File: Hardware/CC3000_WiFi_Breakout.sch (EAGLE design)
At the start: 31 parts, among them J1 U.FL, U1 LM1117, U3 74HC4050, U5 CC3000

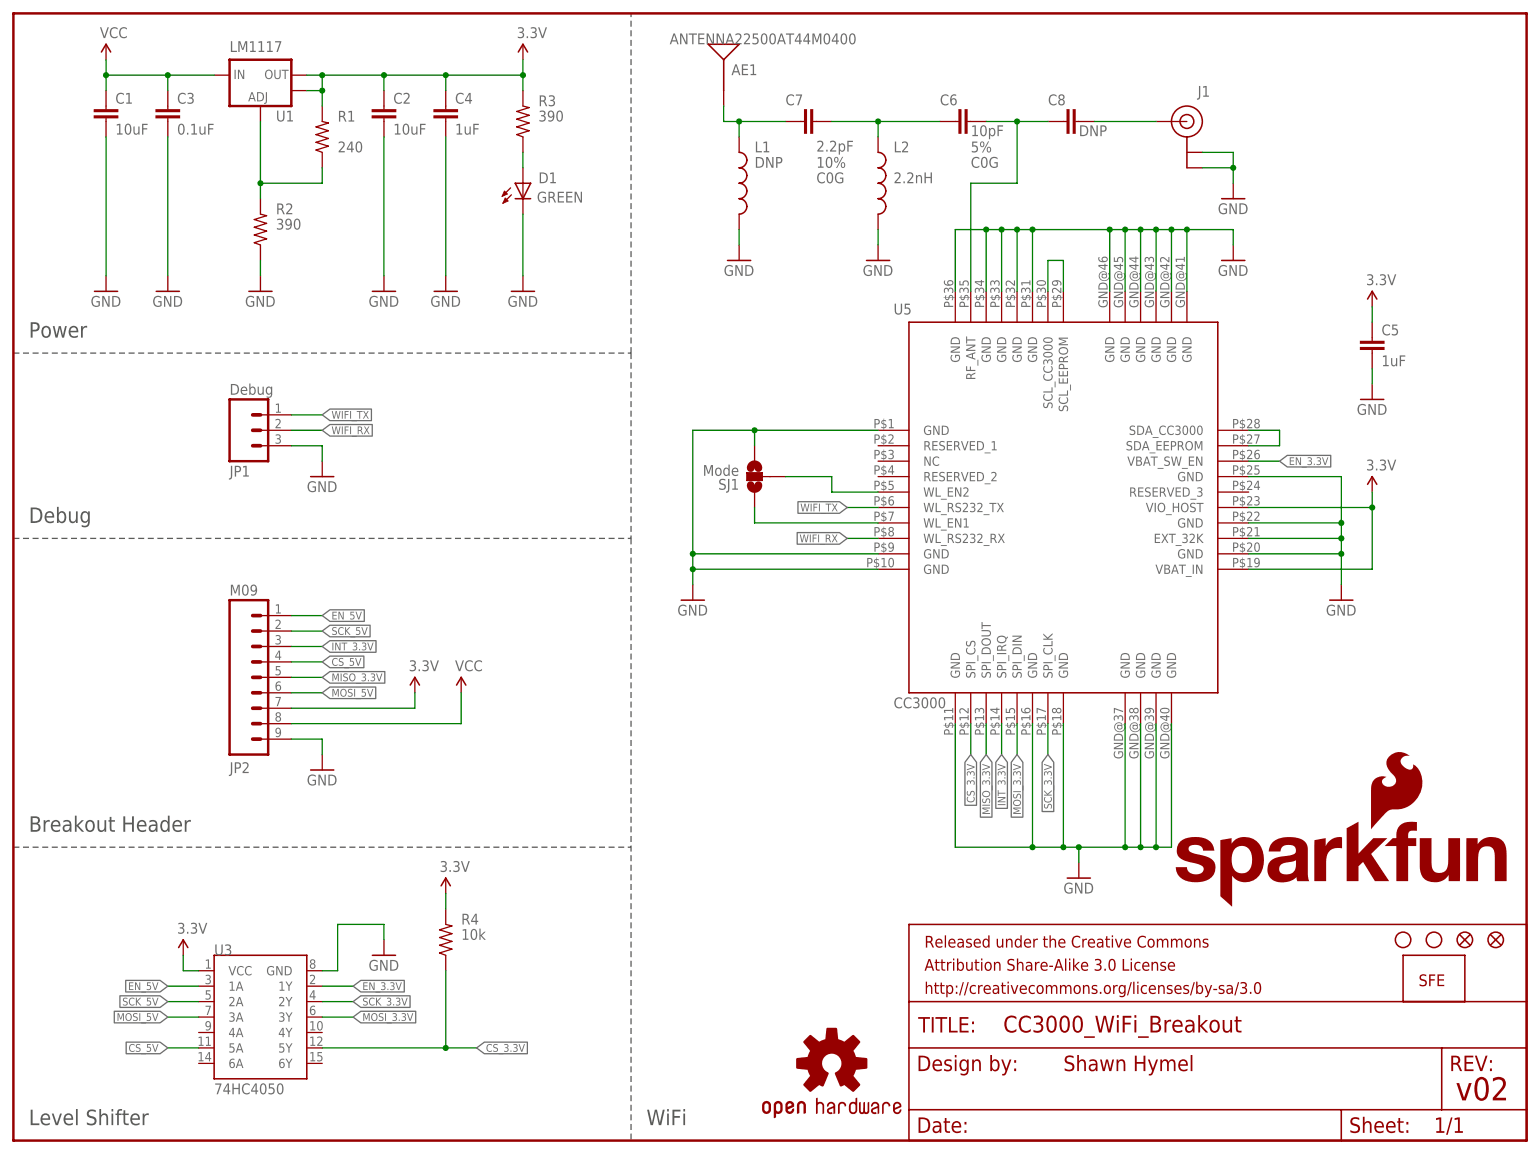
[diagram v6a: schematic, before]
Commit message: Moved SS Flame down, added pin marker for U.FL in SS
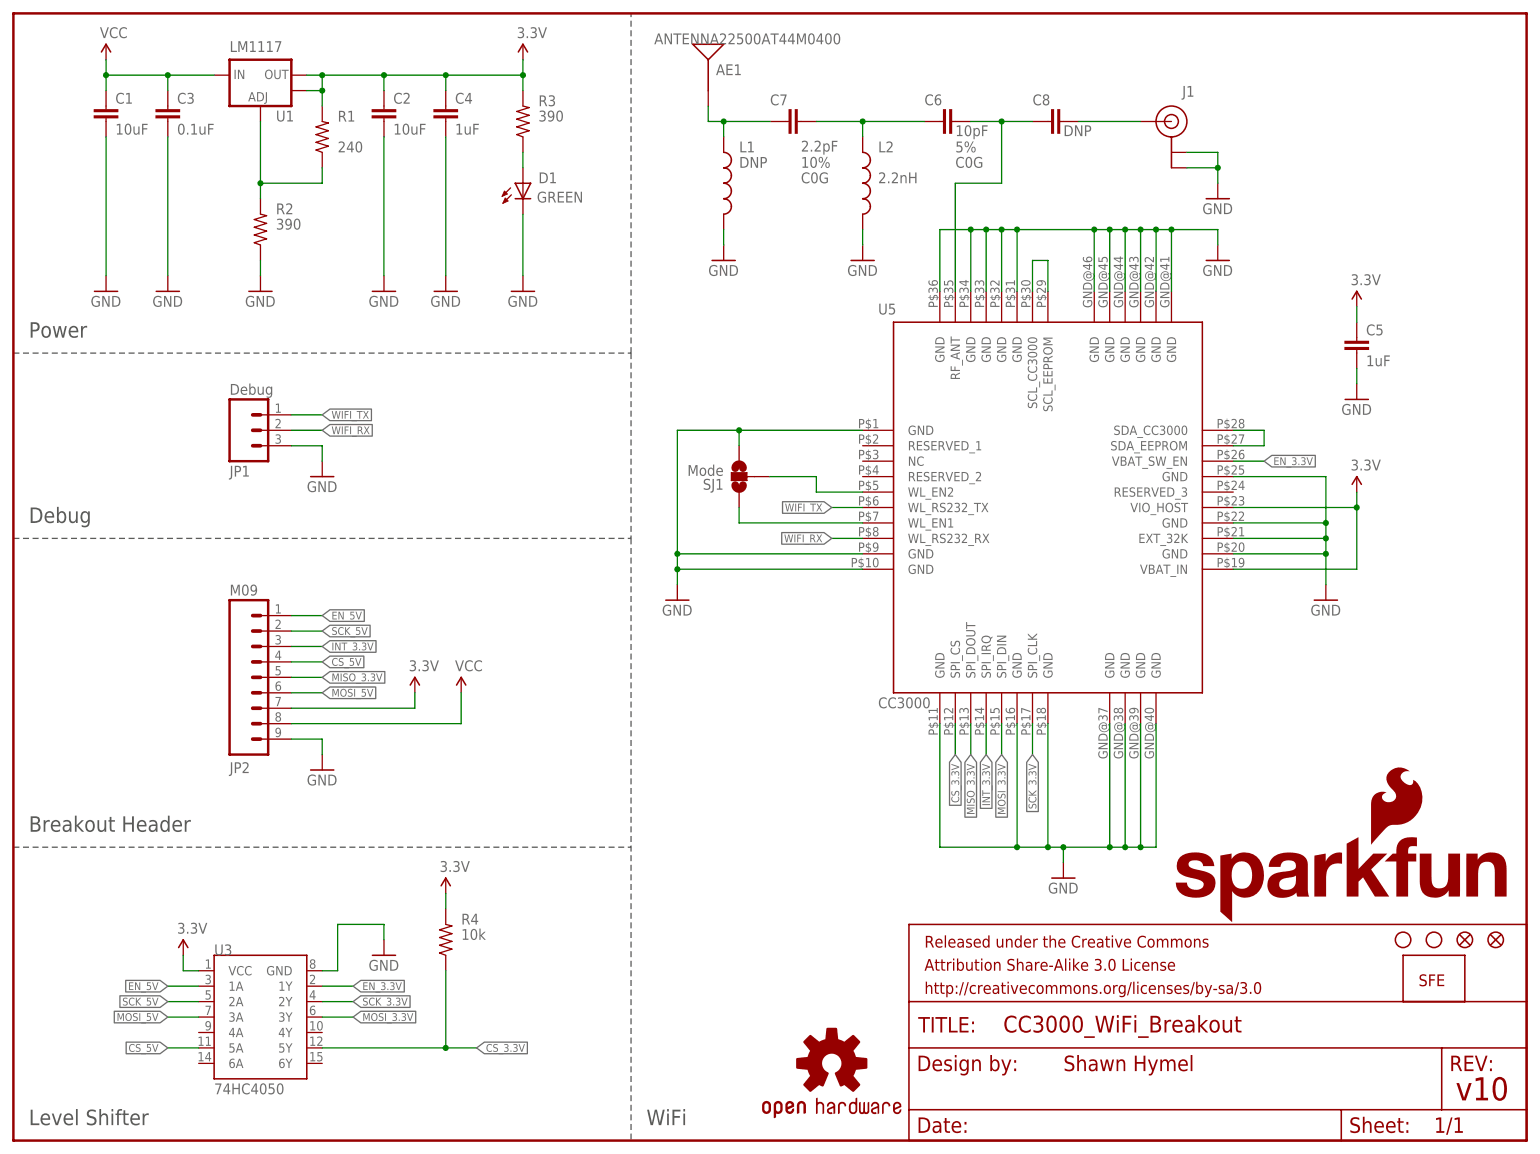
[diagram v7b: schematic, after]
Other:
- note added: "v10"
- note removed: "v02"
- moved on the sheet: AE1, C5, C6, C7, C8, J1, L1, L2, SJ1, U5

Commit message: Added silk U.FL; adjusted tvalue markings for easier reading
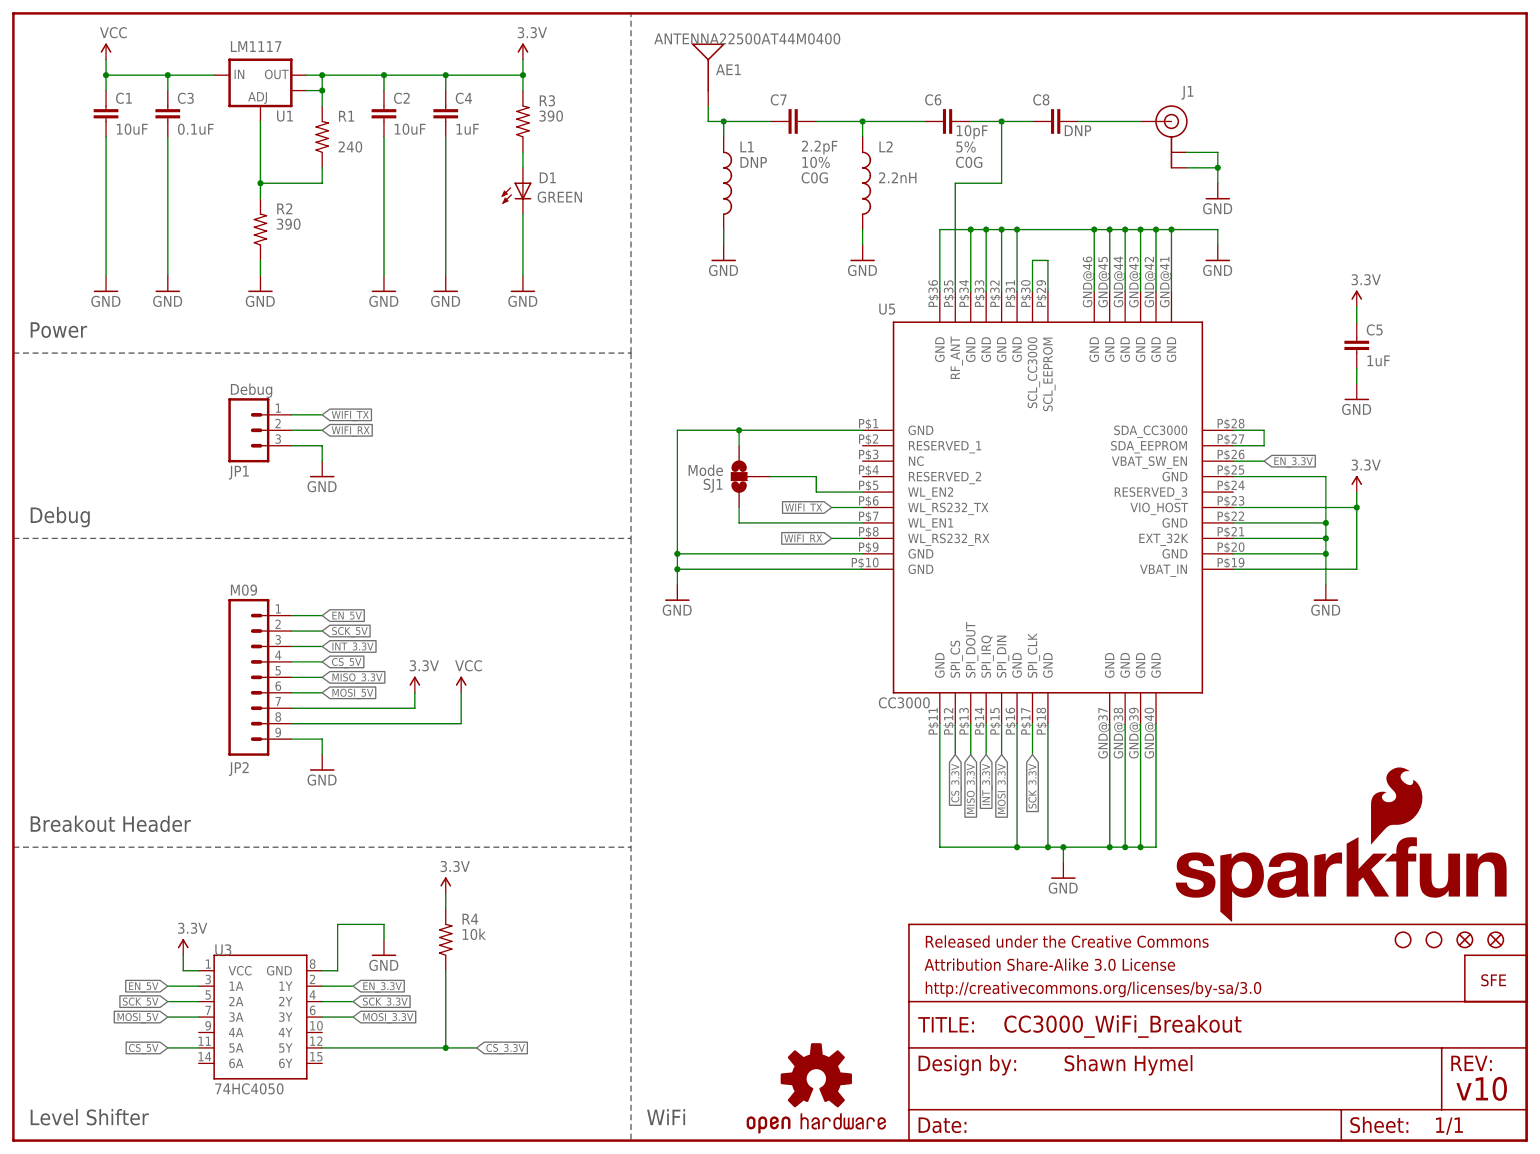
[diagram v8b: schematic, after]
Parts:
- L1: value (none) -> DNP; PLACE DNP -> (none)
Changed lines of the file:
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@@
 <setting verticaltext="up"/>
 </settings>
-<grid distance="0.1" unitdist="inch" unit="inch" style="lines" multiple="1" display="no" altdistance="0.01" altunitdist="inch" altunit="inch"/>
+<grid distance="0.1" unitdist="inch" unit="inch" style="lines" multiple="1" display="yes" altdistance="0.01" altunitdist="inch" altunit="inch"/>
 <layers>
 <layer number="1" name="Top" color="4" fill="1" visible="no" active="no"/>
@@
 <attribute name="TOL" value="5%"/>
 </part>
-<part name="L1" library="SparkFun-Passives" deviceset="INDUCTOR" device="0603">
-<attribute name="PLACE" value="DNP"/>
-</part>
+<part name="L1" library="SparkFun-Passives" deviceset="INDUCTOR" device="0603" value="DNP"/>
 <part name="L2" library="SparkFun-Passives" deviceset="INDUCTOR" device="0603" value="2.2nH"/>
 <part name="GND15" library="SparkFun-Aesthetics" deviceset="GND" device=""/>
@@
 <attribute name="VALUE" x="154.94" y="165.227" size="1.778" layer="96"/>
 </instance>
-<instance part="L1" gate="G$1" x="116.84" y="157.48">
-<attribute name="PLACE" x="119.38" y="160.02" size="1.778" layer="96"/>
+<instance part="L1" gate="G$1" x="116.84" y="157.48" smashed="yes">
+<attribute name="NAME" x="119.38" y="162.56" size="1.778" layer="95"/>
+<attribute name="VALUE" x="119.38" y="160.02" size="1.778" layer="96"/>
 </instance>
 <instance part="L2" gate="G$1" x="139.7" y="157.48" smashed="yes">
@@
 <instance part="FID1" gate="G$1" x="243.84" y="33.02"/>
 <instance part="FID2" gate="G$1" x="238.76" y="33.02"/>
-<instance part="LOGO1" gate="G$1" x="134.62" y="12.7"/>
-<instance part="LOGO3" gate="G$1" x="231.14" y="25.4"/>
+<instance part="LOGO1" gate="G$1" x="132.08" y="10.16"/>
+<instance part="LOGO3" gate="G$1" x="241.3" y="25.4"/>
 <instance part="JP2" gate="G$1" x="35.56" y="76.2" smashed="yes" rot="MR180">
 <attribute name="VALUE" x="35.56" y="91.44" size="1.778" layer="96" rot="MR180"/>
